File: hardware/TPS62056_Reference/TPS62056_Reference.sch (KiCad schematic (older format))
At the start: 16 parts, among them J1 GS2, P1 CONN_5, SW1 SW_ON, SW2 SW_OFF, U1 TPS6205X

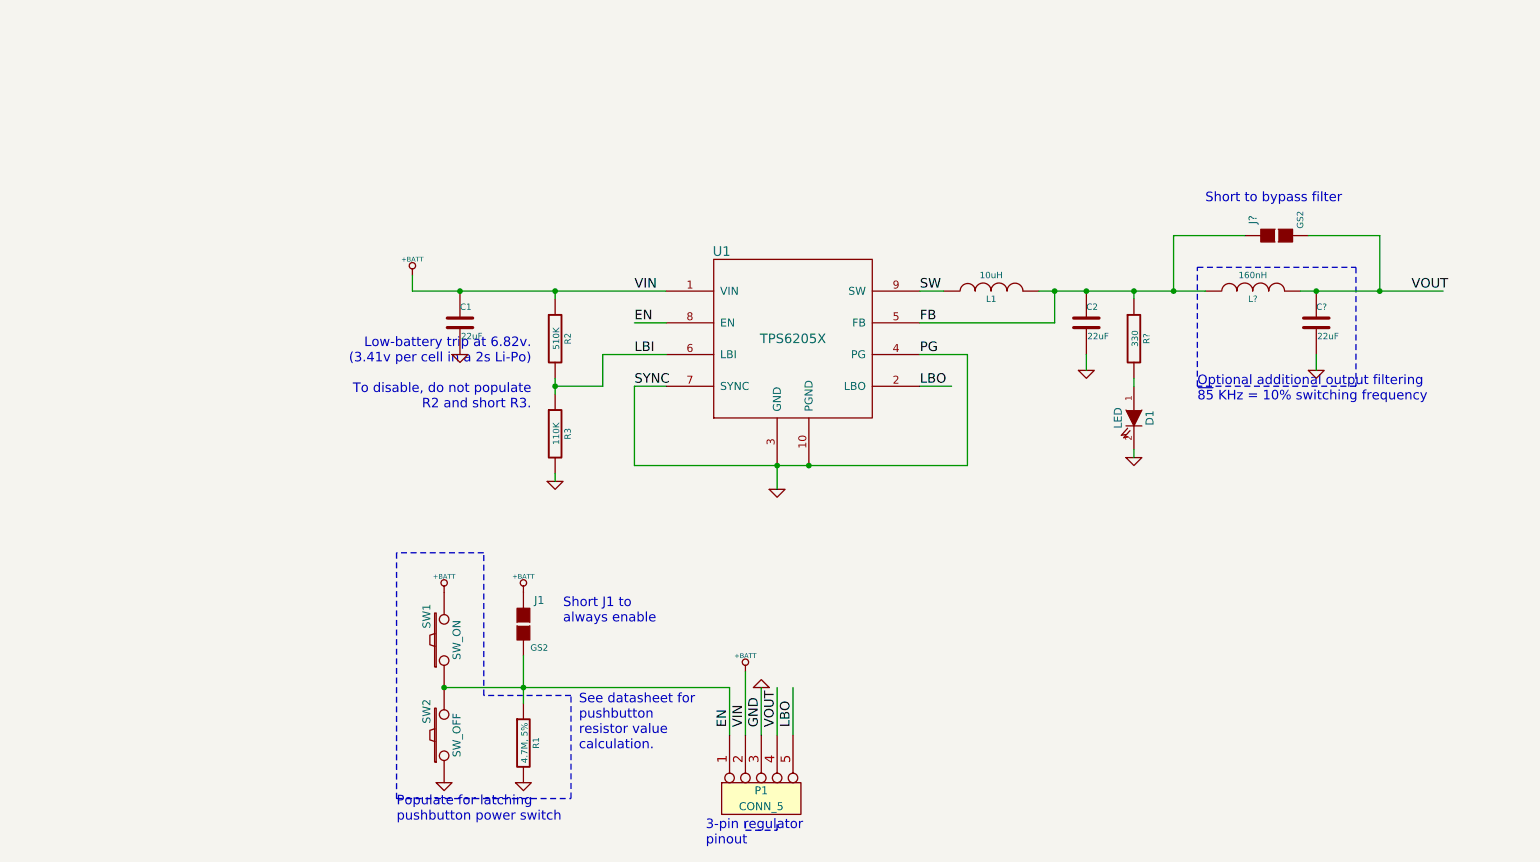
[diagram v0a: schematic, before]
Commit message: Found parts, created footprints, added to board.
Board had all footprints on it, but it completely rat's nest.
Spreadsheet BOM created, but not yet in repo.
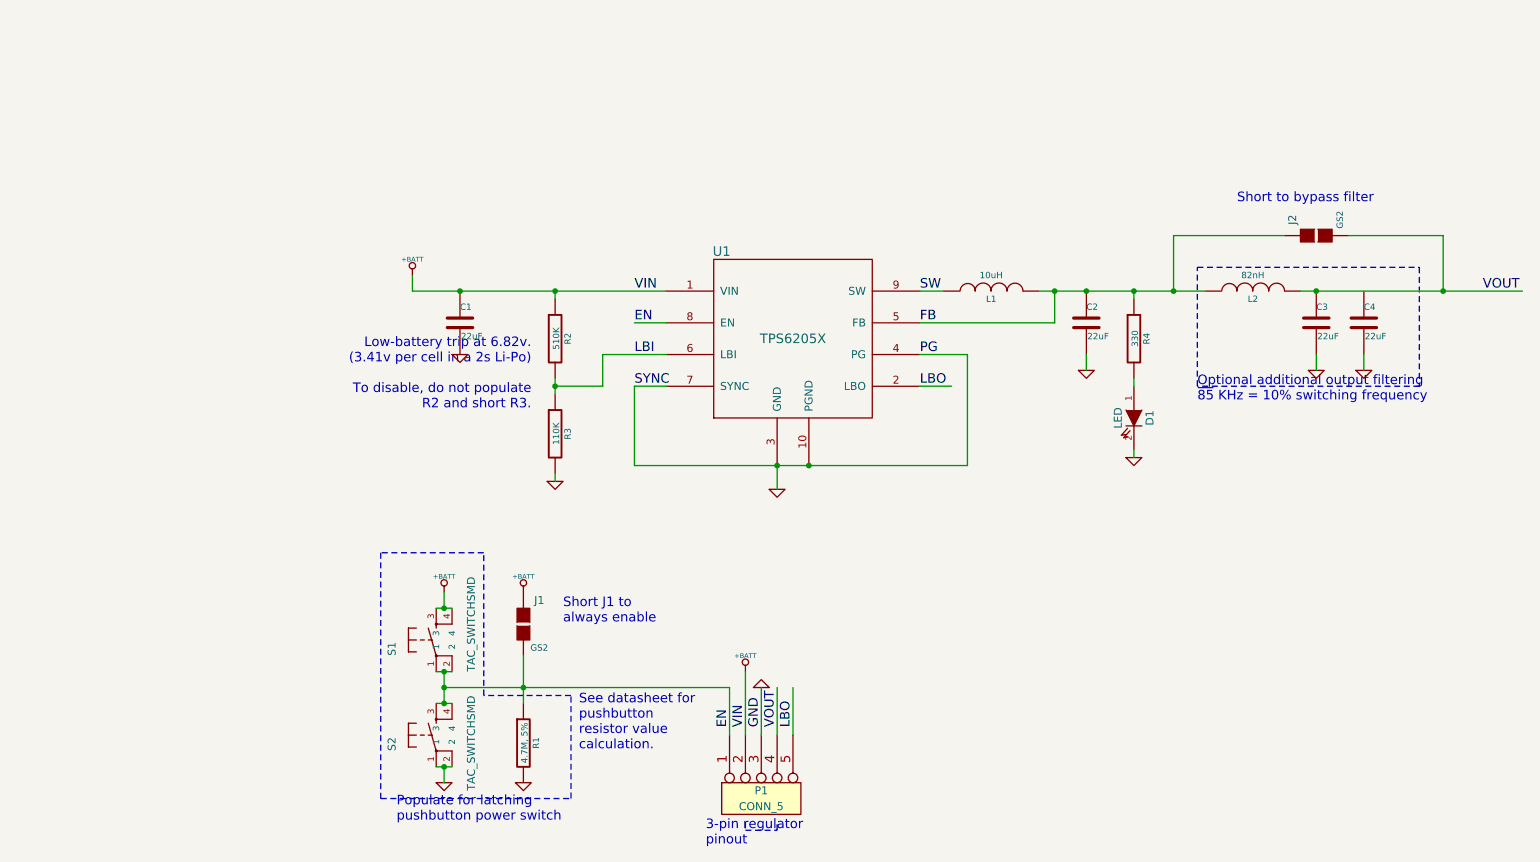
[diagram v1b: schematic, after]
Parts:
- removed SW1: SW_ON, ~, symbol SW_PUSH
- removed SW2: SW_OFF, ~, symbol SW_PUSH
- added C4: 22uF, ~, symbol C
- added S1, S2: TAC_SWITCHSMD, SparkFun-TACTILE_SWITCH_SMD, symbol TAC_SWITCHSMD
- L2: renamed from L?; value 160nH -> 82nH
- gave numbers to parts that had none: 3
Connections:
- wire segments 37 -> 45
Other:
- moved on the sheet: J2
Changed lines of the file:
@@
 LIBS:valves
 LIBS:tps6205x
+LIBS:SparkFun
 LIBS:TPS62056_Reference-cache
 EELAYER 27 0
@@
 Sheet 1 1
 Title "TPS6205x-based Fixed Voltage Switching Regulator Module"
-Date "17 jul 2013"
+Date "23 jul 2013"
 Rev "A"
 Comp "UCR Micromouse"
@@
 $EndComp
 $Comp
-L SW_PUSH SW1
-U 1 1 51E33616
-P 3200 5400
-F 0 "SW1" H 3350 5510 50  0000 C CNN
-F 1 "SW_ON" H 3200 5320 50  0000 C CNN
-F 2 "~" H 3200 5400 60  0000 C CNN
-F 3 "~" H 3200 5400 60  0000 C CNN
-	1    3200 5400
-	0    -1   -1   0
-$EndComp
-$Comp
-L SW_PUSH SW2
-U 1 1 51E33623
-P 3200 6000
-F 0 "SW2" H 3350 6110 50  0000 C CNN
-F 1 "SW_OFF" H 3200 5920 50  0000 C CNN
-F 2 "~" H 3200 6000 60  0000 C CNN
-F 3 "~" H 3200 6000 60  0000 C CNN
-	1    3200 6000
-	0    -1   -1   0
-$EndComp
-$Comp
 L GND #PWR06
 U 1 1 51E3365B
@@
 Text Notes 4850 6700 0    60   ~ 0
 3-pin regulator\npinout
-Wire Wire Line
-	6200 3200 6350 3200
-Wire Wire Line
-	4400 3400 4600 3400
-Wire Wire Line
-	5000 5700 5000 6000
-Wire Wire Line
-	5100 5600 5100 6000
-Wire Wire Line
-	5200 6000 5200 5700
-Wire Wire Line
-	5300 6000 5300 5700
-Wire Wire Line
-	5400 6000 5400 5700
-Wire Wire Line
-	6200 3600 6500 3600
-Wire Wire Line
-	6200 3800 6400 3800
-Wire Wire Line
-	6200 3400 7050 3400
-Wire Wire Line
-	4400 3800 4600 3800
-Wire Wire Line
-	4400 3800 4400 4300
-Wire Wire Line
-	4400 4300 6500 4300
-Wire Wire Line
-	6500 4300 6500 3600
-Connection ~ 5500 4300
-Connection ~ 5300 4300
-Wire Wire Line
-	5300 4300 5300 4450
-Wire Wire Line
-	3200 5700 5000 5700
-Connection ~ 3700 5700
-Wire Wire Line
-	3700 5500 3700 5800
-Wire Notes Line
-	2900 6400 4000 6400
-Wire Notes Line
-	4000 6400 4000 5750
-Wire Notes Line
-	4000 5750 3450 5750
-Wire Notes Line
-	3450 5750 3450 4850
-Wire Notes Line
-	3450 4850 2900 4850
-Wire Notes Line
-	2900 4850 2900 6400
-Connection ~ 3300 3200
-Wire Wire Line
-	7250 3600 7250 3700
-Wire Wire Line
-	3000 3100 3000 3200
-Connection ~ 7250 3200
-Wire Notes Line
-	5100 6550 5100 6600
-Wire Notes Line
-	5100 6600 5300 6600
-Wire Notes Line
-	5300 6600 5300 6550
-Wire Wire Line
-	3000 3200 4600 3200
-Connection ~ 3900 3200
-Wire Wire Line
-	4200 3600 4600 3600
-Wire Wire Line
-	3900 3250 3900 3200
-Wire Wire Line
-	3900 4400 3900 4350
-Wire Wire Line
-	3900 3750 3900 3850
-Wire Wire Line
-	3900 3800 4200 3800
-Wire Wire Line
-	4200 3800 4200 3600
-Connection ~ 3900 3800
-Wire Wire Line
-	6950 3200 8000 3200
-Wire Wire Line
-	7050 3400 7050 3200
-Connection ~ 7050 3200
 $Comp
 L LED D1
@@
 $EndComp
 $Comp
-L R R?
+L R R4
 U 1 1 51E34F4A
 P 7550 3500
-F 0 "R?" V 7630 3500 40  0000 C CNN
+F 0 "R4" V 7630 3500 40  0000 C CNN
 F 1 "330" V 7557 3501 40  0000 C CNN
 F 2 "~" V 7480 3500 30  0000 C CNN
@@
 $EndComp
 $Comp
-L GND #PWR?
+L GND #PWR012
 U 1 1 51E34F59
 P 7550 4250
-F 0 "#PWR?" H 7550 4250 30  0001 C CNN
+F 0 "#PWR012" H 7550 4250 30  0001 C CNN
 F 1 "GND" H 7550 4180 30  0001 C CNN
 F 2 "" H 7550 4250 60  0000 C CNN
@@
 	1    0    0    -1
 $EndComp
-Wire Wire Line
-	7550 4250 7550 4200
-Wire Wire Line
-	7550 3800 7550 3750
-Wire Wire Line
-	7550 3250 7550 3200
-Connection ~ 7550 3200
-Connection ~ 3200 5700
 Text Notes 4050 6100 0    60   ~ 0
 See datasheet for\npushbutton\nresistor value\ncalculation.
 $Comp
-L INDUCTOR L?
+L INDUCTOR L2
 U 1 1 51E6F3B0
 P 8300 3200
-F 0 "L?" V 8250 3200 40  0000 C CNN
-F 1 "160nH" V 8400 3200 40  0000 C CNN
+F 0 "L2" V 8250 3200 40  0000 C CNN
+F 1 "82nH" V 8400 3200 40  0000 C CNN
 F 2 "~" H 8300 3200 60  0000 C CNN
 F 3 "~" H 8300 3200 60  0000 C CNN
@@
 $EndComp
 $Comp
-L C C?
+L C C3
 U 1 1 51E6F3B6
 P 8700 3400
-F 0 "C?" H 8700 3500 40  0000 L CNN
+F 0 "C3" H 8700 3500 40  0000 L CNN
 F 1 "22uF" H 8706 3315 40  0000 L CNN
 F 2 "~" H 8738 3250 30  0000 C CNN
@@
 $EndComp
 $Comp
-L GND #PWR?
+L GND #PWR013
 U 1 1 51E6F3BC
 P 8700 3700
-F 0 "#PWR?" H 8700 3700 30  0001 C CNN
+F 0 "#PWR013" H 8700 3700 30  0001 C CNN
 F 1 "GND" H 8700 3630 30  0001 C CNN
 F 2 "" H 8700 3700 60  0000 C CNN
@@
 	1    0    0    -1
 $EndComp
-Wire Wire Line
-	8600 3200 9500 3200
+Text Label 9750 3200 0    60   ~ 0
+VOUT
+$Comp
+L GS2 J2
+U 1 1 51E6F548
+P 8700 2850
+F 0 "J2" H 8800 3000 50  0000 C CNN
+F 1 "GS2" H 8800 2701 40  0000 C CNN
+F 2 "" H 8700 2850 60  0000 C CNN
+F 3 "" H 8700 2850 60  0000 C CNN
+	1    8700 2850
+	0    -1   -1   0
+$EndComp
+Text Notes 7950 3900 0    60   ~ 0
+Optional additional output filtering\n~85 KHz = 10% switching frequency\n
+Text Notes 8200 2650 0    60   ~ 0
+Short to bypass filter
+$Comp
+L TAC_SWITCHSMD S2
+U 1 1 51EDEB7B
+P 3150 6000
+F 0 "S2" H 3050 6250 50  0000 L BNN
+F 1 "TAC_SWITCHSMD" H 2800 5750 50  0000 L BNN
+F 2 "SparkFun-TACTILE_SWITCH_SMD" H 3350 5700 50  0001 C CNN
+F 3 "" H 3150 6000 60  0000 C CNN
+	1    3150 6000
+	0    -1   -1   0
+$EndComp
+$Comp
+L TAC_SWITCHSMD S1
+U 1 1 51EDEB95
+P 3150 5400
+F 0 "S1" H 3050 5650 50  0000 L BNN
+F 1 "TAC_SWITCHSMD" H 2950 5150 50  0000 L BNN
+F 2 "SparkFun-TACTILE_SWITCH_SMD" H 3350 5100 50  0001 C CNN
+F 3 "" H 3150 5400 60  0000 C CNN
+	1    3150 5400
+	0    -1   -1   0
+$EndComp
+Wire Wire Line
+	6200 3200 6350 3200
+Wire Wire Line
+	4400 3400 4600 3400
+Wire Wire Line
+	5000 5700 5000 6000
+Wire Wire Line
+	5100 5600 5100 6000
+Wire Wire Line
+	5200 6000 5200 5700
+Wire Wire Line
+	5300 6000 5300 5700
+Wire Wire Line
+	5400 6000 5400 5700
+Wire Wire Line
+	6200 3600 6500 3600
+Wire Wire Line
+	6200 3800 6400 3800
+Wire Wire Line
+	6200 3400 7050 3400
+Wire Wire Line
+	4400 3800 4600 3800
+Wire Wire Line
+	4400 3800 4400 4300
+Wire Wire Line
+	4400 4300 6500 4300
+Wire Wire Line
+	6500 4300 6500 3600
+Connection ~ 5500 4300
+Connection ~ 5300 4300
+Wire Wire Line
+	5300 4300 5300 4450
+Wire Wire Line
+	3200 5700 5000 5700
+Connection ~ 3700 5700
+Wire Wire Line
+	3700 5500 3700 5800
+Wire Notes Line
+	2800 6400 4000 6400
+Wire Notes Line
+	4000 6400 4000 5750
+Wire Notes Line
+	4000 5750 3450 5750
+Wire Notes Line
+	3450 5750 3450 4850
+Wire Notes Line
+	3450 4850 2800 4850
+Wire Notes Line
+	2800 4850 2800 6400
+Connection ~ 3300 3200
+Wire Wire Line
+	7250 3600 7250 3700
+Wire Wire Line
+	3000 3100 3000 3200
+Connection ~ 7250 3200
+Wire Notes Line
+	5100 6550 5100 6600
+Wire Notes Line
+	5100 6600 5300 6600
+Wire Notes Line
+	5300 6600 5300 6550
+Wire Wire Line
+	3000 3200 4600 3200
+Connection ~ 3900 3200
+Wire Wire Line
+	4200 3600 4600 3600
+Wire Wire Line
+	3900 3250 3900 3200
+Wire Wire Line
+	3900 4400 3900 4350
+Wire Wire Line
+	3900 3750 3900 3850
+Wire Wire Line
+	3900 3800 4200 3800
+Wire Wire Line
+	4200 3800 4200 3600
+Connection ~ 3900 3800
+Wire Wire Line
+	6950 3200 8000 3200
+Wire Wire Line
+	7050 3400 7050 3200
+Connection ~ 7050 3200
+Wire Wire Line
+	7550 4250 7550 4200
+Wire Wire Line
+	7550 3800 7550 3750
+Wire Wire Line
+	7550 3250 7550 3200
+Connection ~ 7550 3200
+Wire Wire Line
+	8600 3200 10000 3200
 Wire Wire Line
 	8700 3600 8700 3700
 Connection ~ 8700 3200
-Text Label 9300 3200 0    60   ~ 0
-VOUT
-$Comp
-L GS2 J?
-U 1 1 51E6F548
-P 8450 2850
-F 0 "J?" H 8550 3000 50  0000 C CNN
-F 1 "GS2" H 8550 2701 40  0000 C CNN
-F 2 "" H 8450 2850 60  0000 C CNN
-F 3 "" H 8450 2850 60  0000 C CNN
-	1    8450 2850
-	0    -1   -1   0
-$EndComp
-Wire Notes Line
-	7950 3050 8950 3050
-Wire Notes Line
-	8950 3050 8950 3800
-Wire Notes Line
-	8950 3800 7950 3800
+Wire Notes Line
+	7950 3050 9350 3050
+Wire Notes Line
+	9350 3050 9350 3800
+Wire Notes Line
+	9350 3800 7950 3800
 Wire Notes Line
 	7950 3800 7950 3050
 Wire Wire Line
-	8250 2850 7800 2850
+	8500 2850 7800 2850
 Wire Wire Line
 	7800 2850 7800 3200
 Connection ~ 7800 3200
 Wire Wire Line
-	8650 2850 9100 2850
-Wire Wire Line
-	9100 2850 9100 3200
-Connection ~ 9100 3200
-Text Notes 7950 3900 0    60   ~ 0
-Optional additional output filtering\n~85 KHz = 10% switching frequency\n
-Text Notes 8000 2650 0    60   ~ 0
-Short to bypass filter
+	8900 2850 9500 2850
+Connection ~ 9500 3200
+Wire Wire Line
+	3150 5200 3250 5200
+Wire Wire Line
+	3200 5200 3200 5100
+Connection ~ 3200 5200
+Wire Wire Line
+	3150 5600 3250 5600
+Wire Wire Line
+	3200 5600 3200 5800
+Wire Wire Line
+	3150 5800 3250 5800
+Connection ~ 3200 5600
+Connection ~ 3200 5800
+Connection ~ 3200 5700
+Wire Wire Line
+	3150 6200 3250 6200
+Wire Wire Line
+	3200 6200 3200 6300
+Connection ~ 3200 6200
+Wire Wire Line
+	9500 2850 9500 3200
+$Comp
+L C C4
+U 1 1 51EE3CFB
+P 9000 3400
+F 0 "C4" H 9000 3500 40  0000 L CNN
+F 1 "22uF" H 9006 3315 40  0000 L CNN
+F 2 "~" H 9038 3250 30  0000 C CNN
+F 3 "~" H 9000 3400 60  0000 C CNN
+	1    9000 3400
+	1    0    0    -1
+$EndComp
+$Comp
+L GND #PWR014
+U 1 1 51EE3D01
+P 9000 3700
+F 0 "#PWR014" H 9000 3700 30  0001 C CNN
+F 1 "GND" H 9000 3630 30  0001 C CNN
+F 2 "" H 9000 3700 60  0000 C CNN
+F 3 "" H 9000 3700 60  0000 C CNN
+	1    9000 3700
+	1    0    0    -1
+$EndComp
+Wire Wire Line
+	9000 3600 9000 3700
 $EndSCHEMATC

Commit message: Board is almost completely routed
Except for an error that prevents me from connecting anything to the
IC...
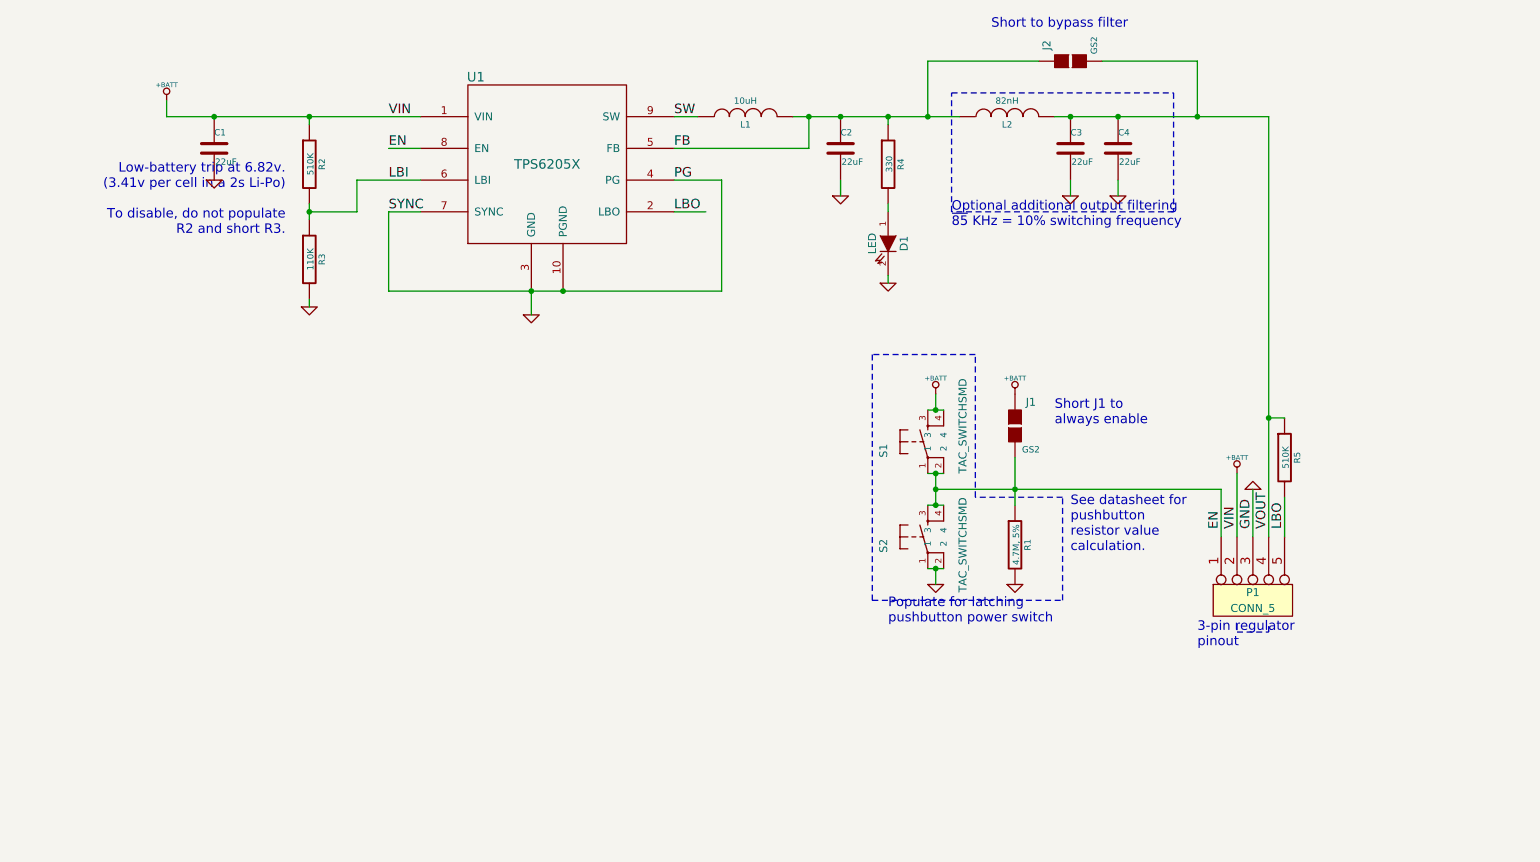
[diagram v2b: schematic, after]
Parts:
- added R5: 510K, ~, symbol R
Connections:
- wire segments 45 -> 46
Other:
- moved on the sheet: C1, C2, C3, C4, D1, J1, J2, L1, L2, P1, R1, R2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
